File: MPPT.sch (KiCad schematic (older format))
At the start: 31 parts, among them U3 SM72442

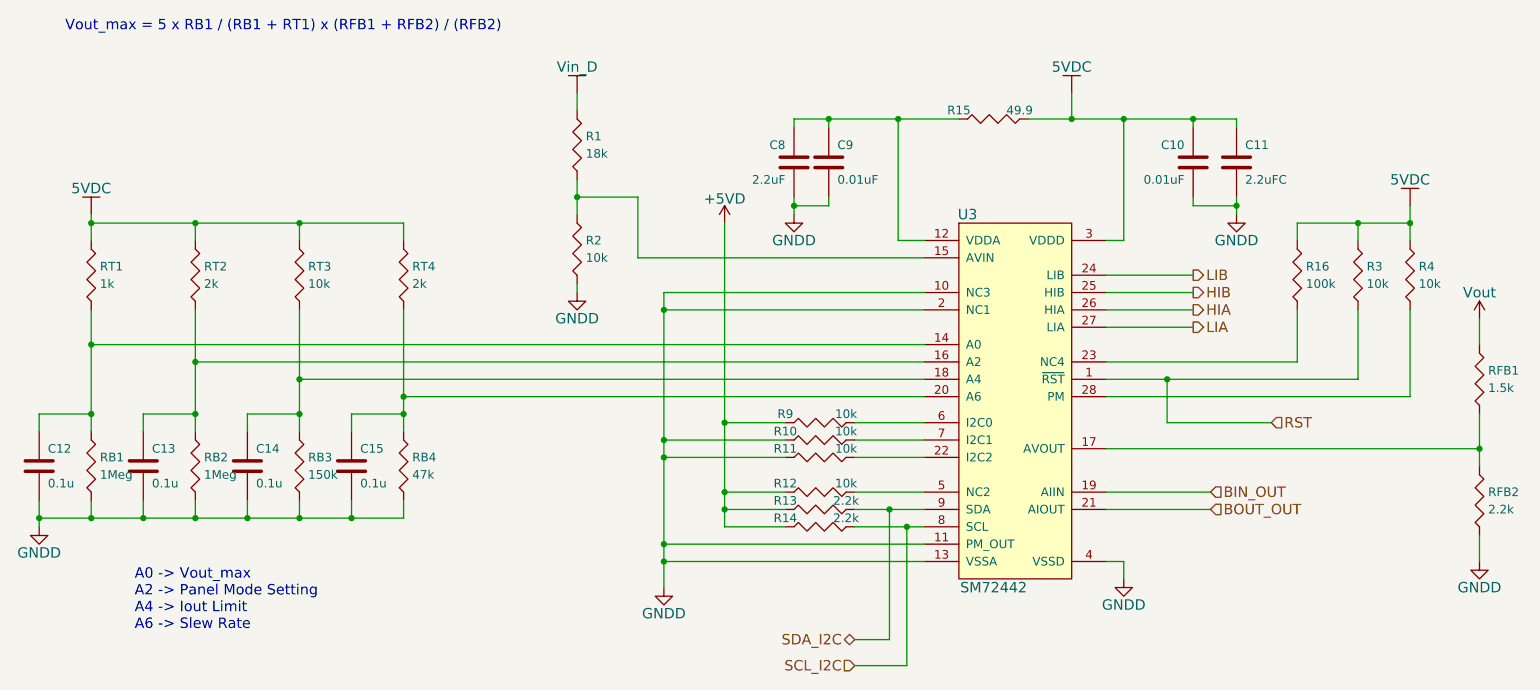
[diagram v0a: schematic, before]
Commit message: Started placing components
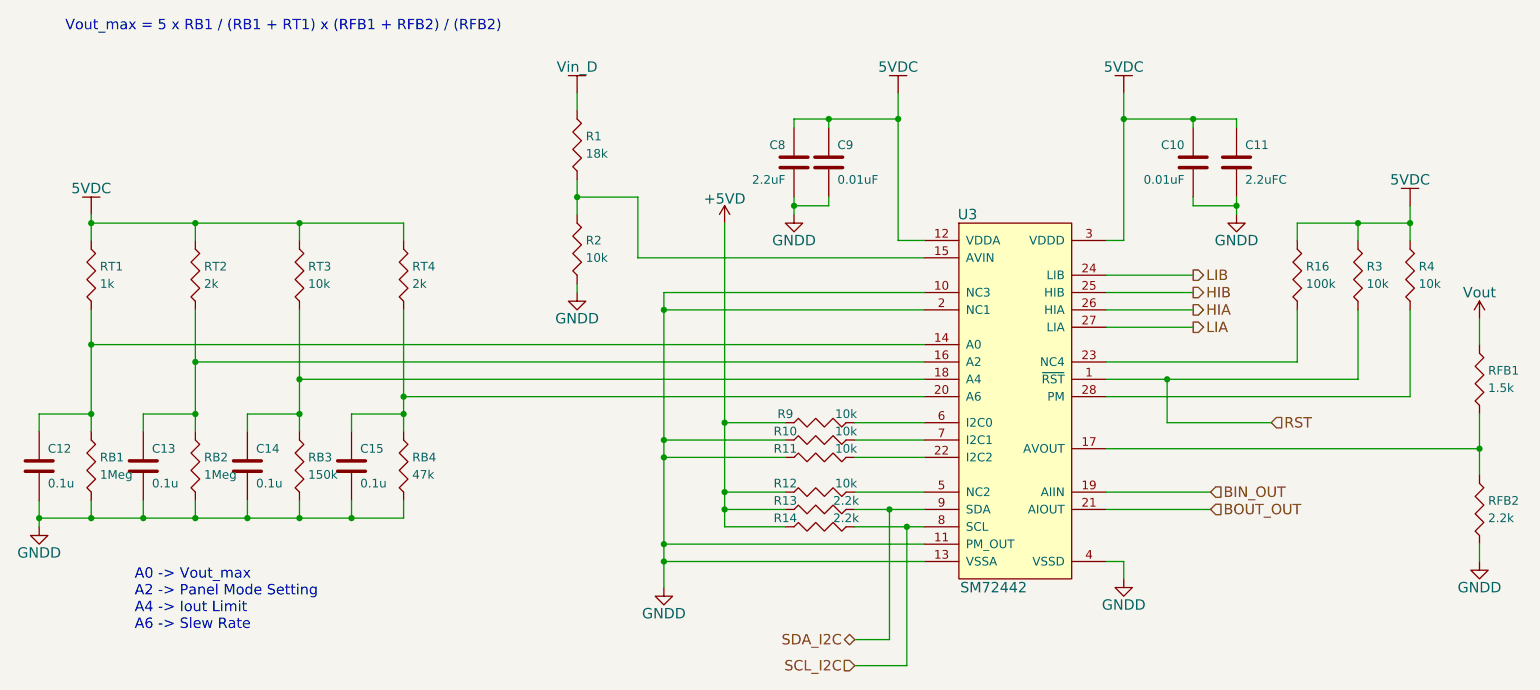
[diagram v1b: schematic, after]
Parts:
- removed R15: 49.9, Resistors_SMD:R_0805_HandSoldering, symbol Rh
- R4: footprint Resistors_SMD:R_0805_HandSoldering -> Resistors_SMD:R_0603_HandSoldering
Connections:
- net 5VDC: now also C8.1, C9.1, U3.12 (VDDA)
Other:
- moved on the sheet: RFB2
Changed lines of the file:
@@
 LIBS:valves
 LIBS:SelfGenerated
+LIBS:ipc-7351-diode
 LIBS:Project_2-cache
 EELAYER 25 0
@@
 	5700 2400 5850 2400
 Wire Wire Line
-	5700 1700 5700 2400
-Wire Wire Line
-	5100 1700 6050 1700
+	5700 1550 5700 2400
+Wire Wire Line
+	5100 1700 5700 1700
 Wire Wire Line
 	5100 1700 5100 1750
@@
 Connection ~ 7400 1700
 Wire Wire Line
-	6900 2400 7000 2400
-Wire Wire Line
-	7000 2400 7000 1700
+	7000 2400 6900 2400
+Wire Wire Line
+	7000 1550 7000 2400
 Connection ~ 7000 1700
-Wire Wire Line
-	6700 1700 6700 1550
-Connection ~ 6700 1700
 Wire Wire Line
 	5100 2150 5100 2250
@@
 Wire Wire Line
 	4200 2500 5850 2500
-$Comp
-L Rh R15
-U 1 1 54EF6978
-P 6250 1700
-F 0 "R15" H 6050 1750 50  0000 C CNN
-F 1 "49.9" H 6400 1750 50  0000 C CNN
-F 2 "Resistors_SMD:R_0805_HandSoldering" H 6250 1630 30  0001 C CNN
-F 3 "" V 6250 1700 30  0000 C CNN
-	1    6250 1700
-	1    0    0    -1
-$EndComp
 Wire Wire Line
 	6900 3100 8000 3100
@@
 F 0 "R4" H 8700 2650 50  0000 L CNN
 F 1 "10k" H 8700 2550 50  0000 L CNN
-F 2 "Resistors_SMD:R_0805_HandSoldering" V 8580 2600 30  0001 C CNN
+F 2 "Resistors_SMD:R_0603_HandSoldering" V 8580 2600 30  0001 C CNN
 F 3 "" H 8650 2600 30  0000 C CNN
 	1    8650 2600
@@
 $EndComp
 Wire Wire Line
-	8350 2800 8350 3200
-Wire Wire Line
-	8350 3200 6900 3200
+	8350 3200 8350 2800
+Wire Wire Line
+	6900 3200 8350 3200
 Wire Wire Line
 	6900 3300 8650 3300
@@
 	8650 3300 8650 2800
 Wire Wire Line
-	6450 1700 7650 1700
+	7000 1700 7650 1700
 Wire Wire Line
 	8000 2400 8000 2300
@@
 L Rv RFB2
 U 1 1 54EF80EA
-P 9050 3900
-F 0 "RFB2" H 9100 3950 50  0000 L CNN
-F 1 "2.2k" H 9100 3850 50  0000 L CNN
-F 2 "Resistors_SMD:R_0805_HandSoldering" V 8980 3900 30  0001 C CNN
-F 3 "" H 9050 3900 30  0000 C CNN
-	1    9050 3900
+P 9050 3950
+F 0 "RFB2" H 9100 4000 50  0000 L CNN
+F 1 "2.2k" H 9100 3900 50  0000 L CNN
+F 2 "Resistors_SMD:R_0805_HandSoldering" V 8980 3950 30  0001 C CNN
+F 3 "" H 9050 3950 30  0000 C CNN
+	1    9050 3950
 	1    0    0    -1
 $EndComp
@@
 	6900 3600 9050 3600
 Wire Wire Line
-	9050 3400 9050 3700
+	9050 3400 9050 3750
 Connection ~ 9050 3600
 $Comp
@@
 $EndComp
 Wire Wire Line
-	9050 4100 9050 4250
+	9050 4150 9050 4250
 $Comp
 L Vout #PWR08
@@
 L 5VDC #PWR011
 U 1 1 54F8C194
-P 6700 1550
-F 0 "#PWR011" H 6700 1400 60  0001 C CNN
-F 1 "5VDC" H 6700 1700 60  0000 C CNN
-F 2 "" H 6700 1550 60  0000 C CNN
-F 3 "" H 6700 1550 60  0000 C CNN
-	1    6700 1550
+P 7000 1550
+F 0 "#PWR011" H 7000 1400 60  0001 C CNN
+F 1 "5VDC" H 7000 1700 60  0000 C CNN
+F 2 "" H 7000 1550 60  0000 C CNN
+F 3 "" H 7000 1550 60  0000 C CNN
+	1    7000 1550
 	1    0    0    -1
 $EndComp
@@
 	1    0    0    -1
 $EndComp
+$Comp
+L 5VDC #PWR014
+U 1 1 54FE3CE7
+P 5700 1550
+F 0 "#PWR014" H 5700 1400 60  0001 C CNN
+F 1 "5VDC" H 5700 1700 60  0000 C CNN
+F 2 "" H 5700 1550 60  0000 C CNN
+F 3 "" H 5700 1550 60  0000 C CNN
+	1    5700 1550
+	1    0    0    -1
+$EndComp

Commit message: still trying to get initial placements done.  Still need to fine-tune
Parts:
- C10, C11, C12, C13, C14, C15, C8, C9: footprint Capacitors_SMD:C_0805_HandSoldering -> Capacitors_SMD:C_0603_HandSoldering
- R1, R10, R11, R12, R13, R14, R16, R2, R3, R9, RB1, RB2, RB3, RB4, RFB1, RFB2, RT1, RT2, RT3, RT4: footprint Resistors_SMD:R_0805_HandSoldering -> Resistors_SMD:R_0603_HandSoldering
- U3: footprint Housings_SOIC:SOIC-28_7.5x17.9mm_Pitch1.27mm -> Housings_SSOP:TSSOP-28_4.4x9.7mm_Pitch0.65mm
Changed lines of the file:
@@
 F 0 "U3" H 6100 3550 60  0000 C CNN
 F 1 "SM72442" H 6250 1400 60  0000 C CNN
-F 2 "Housings_SOIC:SOIC-28_7.5x17.9mm_Pitch1.27mm" H 6350 2900 60  0001 C CNN
+F 2 "Housings_SSOP:TSSOP-28_4.4x9.7mm_Pitch0.65mm" H 6350 2900 60  0001 C CNN
 F 3 "" H 6350 2900 60  0000 C CNN
 	1    6350 2900
@@
 F 0 "C9" H 5350 2050 50  0000 L CNN
 F 1 "0.01uF" H 5350 1850 50  0000 L CNN
-F 2 "Capacitors_SMD:C_0805_HandSoldering" H 5338 1800 30  0001 C CNN
+F 2 "Capacitors_SMD:C_0603_HandSoldering" H 5338 1800 30  0001 C CNN
 F 3 "" H 5300 1950 60  0000 C CNN
 	1    5300 1950
@@
 F 0 "C8" H 5150 2050 50  0000 L CNN
 F 1 "2.2uF" H 5150 1850 50  0000 L CNN
-F 2 "Capacitors_SMD:C_0805_HandSoldering" H 5138 1800 30  0001 C CNN
+F 2 "Capacitors_SMD:C_0603_HandSoldering" H 5138 1800 30  0001 C CNN
 F 3 "" H 5100 1950 60  0000 C CNN
 	1    5100 1950
@@
 F 0 "C10" H 7450 2050 50  0000 L CNN
 F 1 "0.01uF" H 7450 1850 50  0000 L CNN
-F 2 "Capacitors_SMD:C_0805_HandSoldering" H 7438 1800 30  0001 C CNN
+F 2 "Capacitors_SMD:C_0603_HandSoldering" H 7438 1800 30  0001 C CNN
 F 3 "" H 7400 1950 60  0000 C CNN
 	1    7400 1950
@@
 F 0 "C11" H 7700 2050 50  0000 L CNN
 F 1 "2.2uFC" H 7700 1850 50  0000 L CNN
-F 2 "Capacitors_SMD:C_0805_HandSoldering" H 7688 1800 30  0001 C CNN
+F 2 "Capacitors_SMD:C_0603_HandSoldering" H 7688 1800 30  0001 C CNN
 F 3 "" H 7650 1950 60  0000 C CNN
 	1    7650 1950
@@
 F 0 "C12" H 800 3800 50  0000 L CNN
 F 1 "0.1u" H 800 3600 50  0000 L CNN
-F 2 "Capacitors_SMD:C_0805_HandSoldering" H 788 3550 30  0001 C CNN
+F 2 "Capacitors_SMD:C_0603_HandSoldering" H 788 3550 30  0001 C CNN
 F 3 "" H 750 3700 60  0000 C CNN
 	1    750  3700
@@
 F 0 "C13" H 1400 3800 50  0000 L CNN
 F 1 "0.1u" H 1400 3600 50  0000 L CNN
-F 2 "Capacitors_SMD:C_0805_HandSoldering" H 1388 3550 30  0001 C CNN
+F 2 "Capacitors_SMD:C_0603_HandSoldering" H 1388 3550 30  0001 C CNN
 F 3 "" H 1350 3700 60  0000 C CNN
 	1    1350 3700
@@
 F 0 "C14" H 2000 3800 50  0000 L CNN
 F 1 "0.1u" H 2000 3600 50  0000 L CNN
-F 2 "Capacitors_SMD:C_0805_HandSoldering" H 1988 3550 30  0001 C CNN
+F 2 "Capacitors_SMD:C_0603_HandSoldering" H 1988 3550 30  0001 C CNN
 F 3 "" H 1950 3700 60  0000 C CNN
 	1    1950 3700
@@
 F 0 "C15" H 2600 3800 50  0000 L CNN
 F 1 "0.1u" H 2600 3600 50  0000 L CNN
-F 2 "Capacitors_SMD:C_0805_HandSoldering" H 2588 3550 30  0001 C CNN
+F 2 "Capacitors_SMD:C_0603_HandSoldering" H 2588 3550 30  0001 C CNN
 F 3 "" H 2550 3700 60  0000 C CNN
 	1    2550 3700
@@
 F 0 "RT1" H 1100 2650 50  0000 L CNN
 F 1 "1k" H 1100 2550 50  0000 L CNN
-F 2 "Resistors_SMD:R_0805_HandSoldering" V 980 2600 30  0001 C CNN
+F 2 "Resistors_SMD:R_0603_HandSoldering" V 980 2600 30  0001 C CNN
 F 3 "" H 1050 2600 30  0000 C CNN
 	1    1050 2600
@@
 F 0 "RT2" H 1700 2650 50  0000 L CNN
 F 1 "2k" H 1700 2550 50  0000 L CNN
-F 2 "Resistors_SMD:R_0805_HandSoldering" V 1580 2600 30  0001 C CNN
+F 2 "Resistors_SMD:R_0603_HandSoldering" V 1580 2600 30  0001 C CNN
 F 3 "" H 1650 2600 30  0000 C CNN
 	1    1650 2600
@@
 F 0 "RT3" H 2300 2650 50  0000 L CNN
 F 1 "10k" H 2300 2550 50  0000 L CNN
-F 2 "Resistors_SMD:R_0805_HandSoldering" V 2180 2600 30  0001 C CNN
+F 2 "Resistors_SMD:R_0603_HandSoldering" V 2180 2600 30  0001 C CNN
 F 3 "" H 2250 2600 30  0000 C CNN
 	1    2250 2600
@@
 F 0 "RT4" H 2900 2650 50  0000 L CNN
 F 1 "2k" H 2900 2550 50  0000 L CNN
-F 2 "Resistors_SMD:R_0805_HandSoldering" V 2780 2600 30  0001 C CNN
+F 2 "Resistors_SMD:R_0603_HandSoldering" V 2780 2600 30  0001 C CNN
 F 3 "" H 2850 2600 30  0000 C CNN
 	1    2850 2600
@@
 F 0 "RB1" H 1100 3750 50  0000 L CNN
 F 1 "1Meg" H 1100 3650 50  0000 L CNN
-F 2 "Resistors_SMD:R_0805_HandSoldering" V 980 3700 30  0001 C CNN
+F 2 "Resistors_SMD:R_0603_HandSoldering" V 980 3700 30  0001 C CNN
 F 3 "" H 1050 3700 30  0000 C CNN
 	1    1050 3700
@@
 F 0 "RB2" H 1700 3750 50  0000 L CNN
 F 1 "1Meg" H 1700 3650 50  0000 L CNN
-F 2 "Resistors_SMD:R_0805_HandSoldering" V 1580 3700 30  0001 C CNN
+F 2 "Resistors_SMD:R_0603_HandSoldering" V 1580 3700 30  0001 C CNN
 F 3 "" H 1650 3700 30  0000 C CNN
 	1    1650 3700
@@
 F 0 "RB3" H 2300 3750 50  0000 L CNN
 F 1 "150k" H 2300 3650 50  0000 L CNN
-F 2 "Resistors_SMD:R_0805_HandSoldering" V 2180 3700 30  0001 C CNN
+F 2 "Resistors_SMD:R_0603_HandSoldering" V 2180 3700 30  0001 C CNN
 F 3 "" H 2250 3700 30  0000 C CNN
 	1    2250 3700
@@
 F 0 "RB4" H 2900 3750 50  0000 L CNN
 F 1 "47k" H 2900 3650 50  0000 L CNN
-F 2 "Resistors_SMD:R_0805_HandSoldering" V 2780 3700 30  0001 C CNN
+F 2 "Resistors_SMD:R_0603_HandSoldering" V 2780 3700 30  0001 C CNN
 F 3 "" H 2850 3700 30  0000 C CNN
 	1    2850 3700
@@
 F 0 "R9" H 5050 3500 50  0000 C CNN
 F 1 "10k" H 5400 3500 50  0000 C CNN
-F 2 "Resistors_SMD:R_0805_HandSoldering" H 5250 3380 30  0001 C CNN
+F 2 "Resistors_SMD:R_0603_HandSoldering" H 5250 3380 30  0001 C CNN
 F 3 "" V 5250 3450 30  0000 C CNN
 	1    5250 3450
@@
 F 0 "R12" H 5050 3900 50  0000 C CNN
 F 1 "10k" H 5400 3900 50  0000 C CNN
-F 2 "Resistors_SMD:R_0805_HandSoldering" H 5250 3780 30  0001 C CNN
+F 2 "Resistors_SMD:R_0603_HandSoldering" H 5250 3780 30  0001 C CNN
 F 3 "" V 5250 3850 30  0000 C CNN
 	1    5250 3850
@@
 F 0 "R13" H 5050 4000 50  0000 C CNN
 F 1 "2.2k" H 5400 4000 50  0000 C CNN
-F 2 "Resistors_SMD:R_0805_HandSoldering" H 5250 3880 30  0001 C CNN
+F 2 "Resistors_SMD:R_0603_HandSoldering" H 5250 3880 30  0001 C CNN
 F 3 "" V 5250 3950 30  0000 C CNN
 	1    5250 3950
@@
 F 0 "R14" H 5050 4100 50  0000 C CNN
 F 1 "2.2k" H 5400 4100 50  0000 C CNN
-F 2 "Resistors_SMD:R_0805_HandSoldering" H 5250 3980 30  0001 C CNN
+F 2 "Resistors_SMD:R_0603_HandSoldering" H 5250 3980 30  0001 C CNN
 F 3 "" V 5250 4050 30  0000 C CNN
 	1    5250 4050
@@
 F 0 "R10" H 5050 3600 50  0000 C CNN
 F 1 "10k" H 5400 3600 50  0000 C CNN
-F 2 "Resistors_SMD:R_0805_HandSoldering" H 5250 3480 30  0001 C CNN
+F 2 "Resistors_SMD:R_0603_HandSoldering" H 5250 3480 30  0001 C CNN
 F 3 "" V 5250 3550 30  0000 C CNN
 	1    5250 3550
@@
 F 0 "R11" H 5050 3700 50  0000 C CNN
 F 1 "10k" H 5400 3700 50  0000 C CNN
-F 2 "Resistors_SMD:R_0805_HandSoldering" H 5250 3580 30  0001 C CNN
+F 2 "Resistors_SMD:R_0603_HandSoldering" H 5250 3580 30  0001 C CNN
 F 3 "" V 5250 3650 30  0000 C CNN
 	1    5250 3650
@@
 F 0 "R16" H 8050 2650 50  0000 L CNN
 F 1 "100k" H 8050 2550 50  0000 L CNN
-F 2 "Resistors_SMD:R_0805_HandSoldering" V 7930 2600 30  0001 C CNN
+F 2 "Resistors_SMD:R_0603_HandSoldering" V 7930 2600 30  0001 C CNN
 F 3 "" H 8000 2600 30  0000 C CNN
 	1    8000 2600
@@
 F 0 "R3" H 8400 2650 50  0000 L CNN
 F 1 "10k" H 8400 2550 50  0000 L CNN
-F 2 "Resistors_SMD:R_0805_HandSoldering" V 8280 2600 30  0001 C CNN
+F 2 "Resistors_SMD:R_0603_HandSoldering" V 8280 2600 30  0001 C CNN
 F 3 "" H 8350 2600 30  0000 C CNN
 	1    8350 2600
@@
 F 0 "RFB1" H 9100 3250 50  0000 L CNN
 F 1 "1.5k" H 9100 3150 50  0000 L CNN
-F 2 "Resistors_SMD:R_0805_HandSoldering" V 8980 3200 30  0001 C CNN
+F 2 "Resistors_SMD:R_0603_HandSoldering" V 8980 3200 30  0001 C CNN
 F 3 "" H 9050 3200 30  0000 C CNN
 	1    9050 3200
@@
 F 0 "RFB2" H 9100 4000 50  0000 L CNN
 F 1 "2.2k" H 9100 3900 50  0000 L CNN
-F 2 "Resistors_SMD:R_0805_HandSoldering" V 8980 3950 30  0001 C CNN
+F 2 "Resistors_SMD:R_0603_HandSoldering" V 8980 3950 30  0001 C CNN
 F 3 "" H 9050 3950 30  0000 C CNN
 	1    9050 3950
@@
 F 0 "R2" H 3900 2500 50  0000 L CNN
 F 1 "10k" H 3900 2400 50  0000 L CNN
-F 2 "Resistors_SMD:R_0805_HandSoldering" V 3780 2450 30  0001 C CNN
+F 2 "Resistors_SMD:R_0603_HandSoldering" V 3780 2450 30  0001 C CNN
 F 3 "" H 3850 2450 30  0000 C CNN
 	1    3850 2450
@@
 F 0 "R1" H 3900 1900 50  0000 L CNN
 F 1 "18k" H 3900 1800 50  0000 L CNN
-F 2 "Resistors_SMD:R_0805_HandSoldering" V 3780 1850 30  0001 C CNN
+F 2 "Resistors_SMD:R_0603_HandSoldering" V 3780 1850 30  0001 C CNN
 F 3 "" H 3850 1850 30  0000 C CNN
 	1    3850 1850

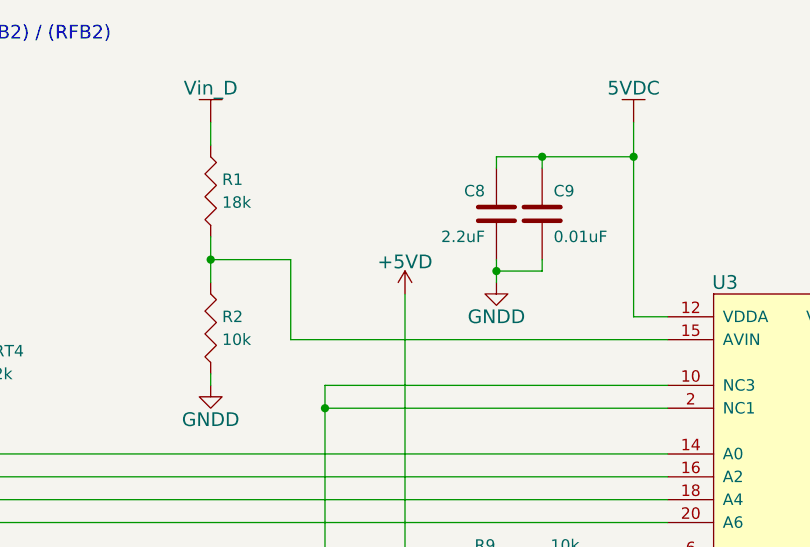
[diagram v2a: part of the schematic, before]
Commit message: Started routing and dicing up power planes
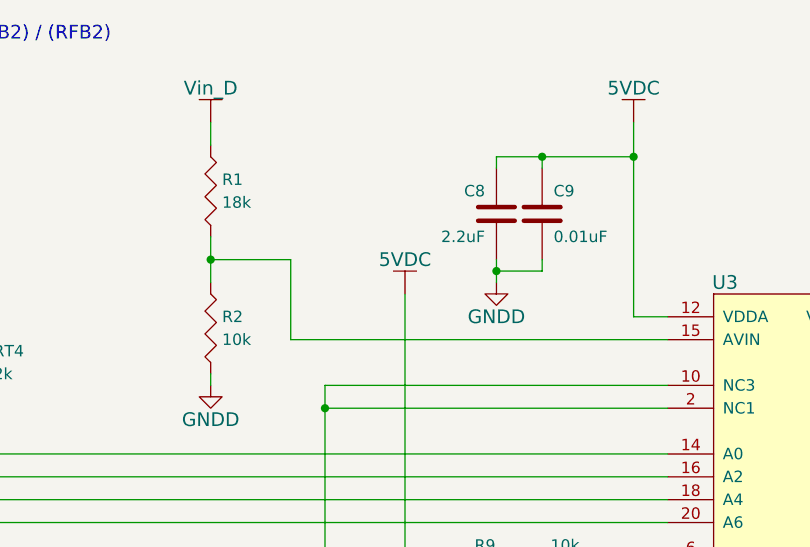
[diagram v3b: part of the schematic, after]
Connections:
- net +5VD is gone; now on net 5VDC: R12.1, R13.1, R14.1, R9.1
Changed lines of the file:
@@
-$EndComp
-$Comp
-L +5VD #PWR01
-U 1 1 54EE2D09
-P 4700 2300
-F 0 "#PWR01" H 4700 2150 60  0001 C CNN
-F 1 "+5VD" H 4700 2440 60  0000 C CNN
-F 2 "" H 4700 2300 60  0000 C CNN
-F 3 "" H 4700 2300 60  0000 C CNN
-	1    4700 2300
-	1    0    0    -1
 $EndComp
 $Comp
@@
 $EndComp
 $Comp
-L GNDD #PWR02
+L GNDD #PWR01
 U 1 1 54EE39BC
 P 5100 2250
-F 0 "#PWR02" H 5100 2000 60  0001 C CNN
+F 0 "#PWR01" H 5100 2000 60  0001 C CNN
 F 1 "GNDD" H 5100 2100 60  0000 C CNN
 F 2 "" H 5100 2250 60  0000 C CNN
@@
 $EndComp
 $Comp
-L GNDD #PWR03
+L GNDD #PWR02
 U 1 1 54EE39DA
 P 7650 2250
-F 0 "#PWR03" H 7650 2000 60  0001 C CNN
+F 0 "#PWR02" H 7650 2000 60  0001 C CNN
 F 1 "GNDD" H 7650 2100 60  0000 C CNN
 F 2 "" H 7650 2250 60  0000 C CNN
@@
 $EndComp
 $Comp
-L GNDD #PWR04
+L GNDD #PWR03
 U 1 1 54EE40C3
 P 4350 4400
-F 0 "#PWR04" H 4350 4150 60  0001 C CNN
+F 0 "#PWR03" H 4350 4150 60  0001 C CNN
 F 1 "GNDD" H 4350 4250 60  0000 C CNN
 F 2 "" H 4350 4400 60  0000 C CNN
@@
 Connection ~ 1650 2300
 $Comp
-L GNDD #PWR05
+L GNDD #PWR04
 U 1 1 54EE6C7A
 P 750 4050
-F 0 "#PWR05" H 750 3800 60  0001 C CNN
+F 0 "#PWR04" H 750 3800 60  0001 C CNN
 F 1 "GNDD" H 750 3900 60  0000 C CNN
 F 2 "" H 750 4050 60  0000 C CNN
@@
 	8000 3100 8000 2800
 $Comp
-L GNDD #PWR06
+L GNDD #PWR05
 U 1 1 54EF74EB
 P 7000 4350
-F 0 "#PWR06" H 7000 4100 60  0001 C CNN
+F 0 "#PWR05" H 7000 4100 60  0001 C CNN
 F 1 "GNDD" H 7000 4200 60  0000 C CNN
 F 2 "" H 7000 4350 60  0000 C CNN
@@
 Connection ~ 9050 3600
 $Comp
-L GNDD #PWR07
+L GNDD #PWR06
 U 1 1 54EF82C6
 P 9050 4250
-F 0 "#PWR07" H 9050 4000 60  0001 C CNN
+F 0 "#PWR06" H 9050 4000 60  0001 C CNN
 F 1 "GNDD" H 9050 4100 60  0000 C CNN
 F 2 "" H 9050 4250 60  0000 C CNN
@@
 	9050 4150 9050 4250
 $Comp
-L Vout #PWR08
+L Vout #PWR07
 U 1 1 54EF84D8
 P 9050 2850
-F 0 "#PWR08" H 9050 2700 60  0001 C CNN
+F 0 "#PWR07" H 9050 2700 60  0001 C CNN
 F 1 "Vout" H 9050 3000 60  0000 C CNN
 F 2 "" H 9050 2850 60  0000 C CNN
@@
 Connection ~ 3850 2150
 $Comp
-L GNDD #PWR09
+L GNDD #PWR08
 U 1 1 54F0CCB7
 P 3850 2700
-F 0 "#PWR09" H 3850 2450 60  0001 C CNN
+F 0 "#PWR08" H 3850 2450 60  0001 C CNN
 F 1 "GNDD" H 3850 2550 60  0000 C CNN
 F 2 "" H 3850 2700 60  0000 C CNN
@@
 Connection ~ 2850 3300
 $Comp
-L 5VDC #PWR010
+L 5VDC #PWR09
 U 1 1 54F8C163
 P 1050 2250
-F 0 "#PWR010" H 1050 2100 60  0001 C CNN
+F 0 "#PWR09" H 1050 2100 60  0001 C CNN
 F 1 "5VDC" H 1050 2400 60  0000 C CNN
 F 2 "" H 1050 2250 60  0000 C CNN
@@
 $EndComp
 $Comp
-L 5VDC #PWR011
+L 5VDC #PWR010
 U 1 1 54F8C194
 P 7000 1550
-F 0 "#PWR011" H 7000 1400 60  0001 C CNN
+F 0 "#PWR010" H 7000 1400 60  0001 C CNN
 F 1 "5VDC" H 7000 1700 60  0000 C CNN
 F 2 "" H 7000 1550 60  0000 C CNN
@@
 $EndComp
 $Comp
-L 5VDC #PWR012
+L 5VDC #PWR011
 U 1 1 54F8C1C3
 P 8650 2200
-F 0 "#PWR012" H 8650 2050 60  0001 C CNN
+F 0 "#PWR011" H 8650 2050 60  0001 C CNN
 F 1 "5VDC" H 8650 2350 60  0000 C CNN
 F 2 "" H 8650 2200 60  0000 C CNN
@@
 $EndComp
 $Comp
-L Vin_D #PWR013
+L Vin_D #PWR012
 U 1 1 54F9D64E
 P 3850 1550
-F 0 "#PWR013" H 3850 1400 60  0001 C CNN
+F 0 "#PWR012" H 3850 1400 60  0001 C CNN
 F 1 "Vin_D" H 3850 1700 60  0000 C CNN
 F 2 "" H 3850 1550 60  0000 C CNN
@@
 $EndComp
 $Comp
-L 5VDC #PWR014
+L 5VDC #PWR013
 U 1 1 54FE3CE7
 P 5700 1550
-F 0 "#PWR014" H 5700 1400 60  0001 C CNN
+F 0 "#PWR013" H 5700 1400 60  0001 C CNN
 F 1 "5VDC" H 5700 1700 60  0000 C CNN
 F 2 "" H 5700 1550 60  0000 C CNN
@@
 	1    0    0    -1
 $EndComp
+$Comp
+L 5VDC #PWR014
+U 1 1 5500A247
+P 4700 2300
+F 0 "#PWR014" H 4700 2150 60  0001 C CNN
+F 1 "5VDC" H 4700 2450 60  0000 C CNN
+F 2 "" H 4700 2300 60  0000 C CNN
+F 3 "" H 4700 2300 60  0000 C CNN
+	1    4700 2300
+	1    0    0    -1
+$EndComp
